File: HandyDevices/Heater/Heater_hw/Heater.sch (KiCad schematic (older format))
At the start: 41 parts

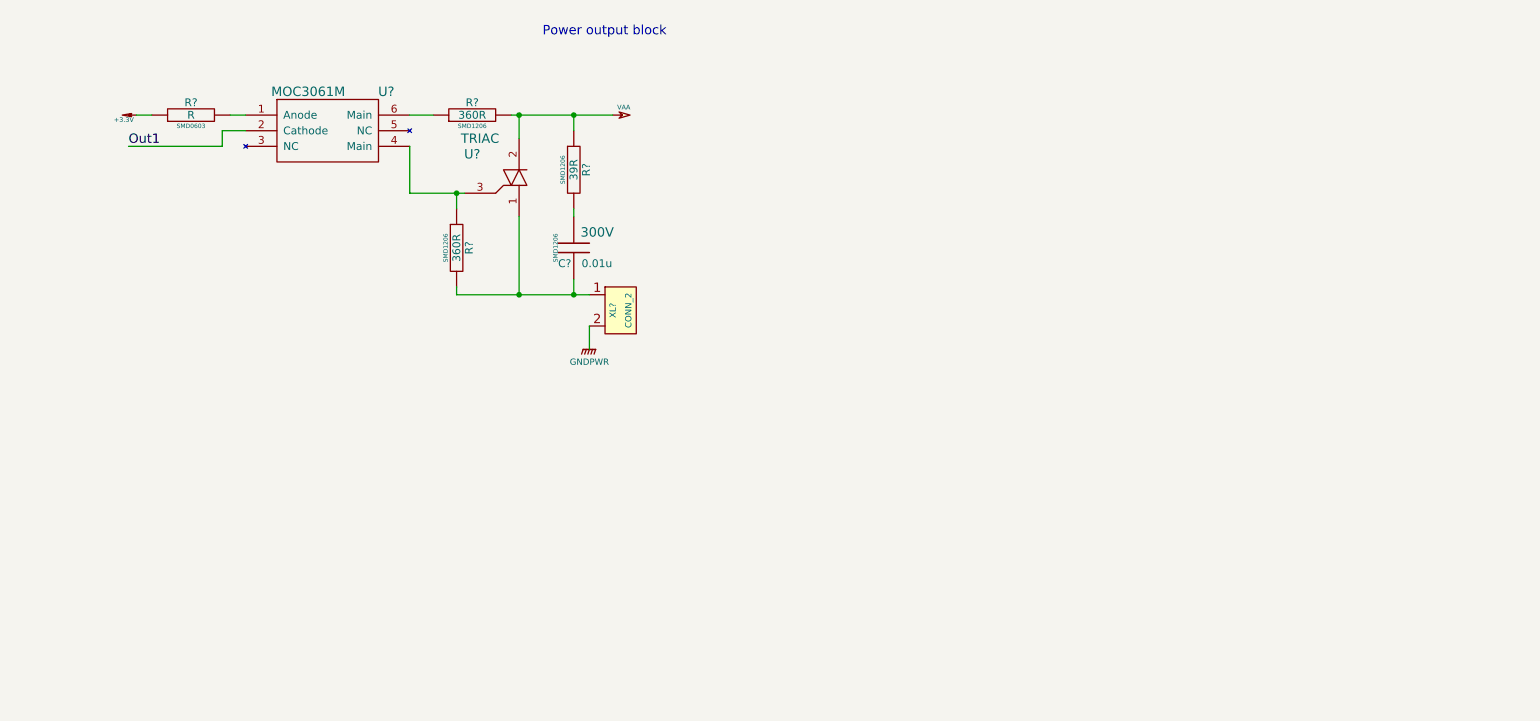
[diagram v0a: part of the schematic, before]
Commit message: 
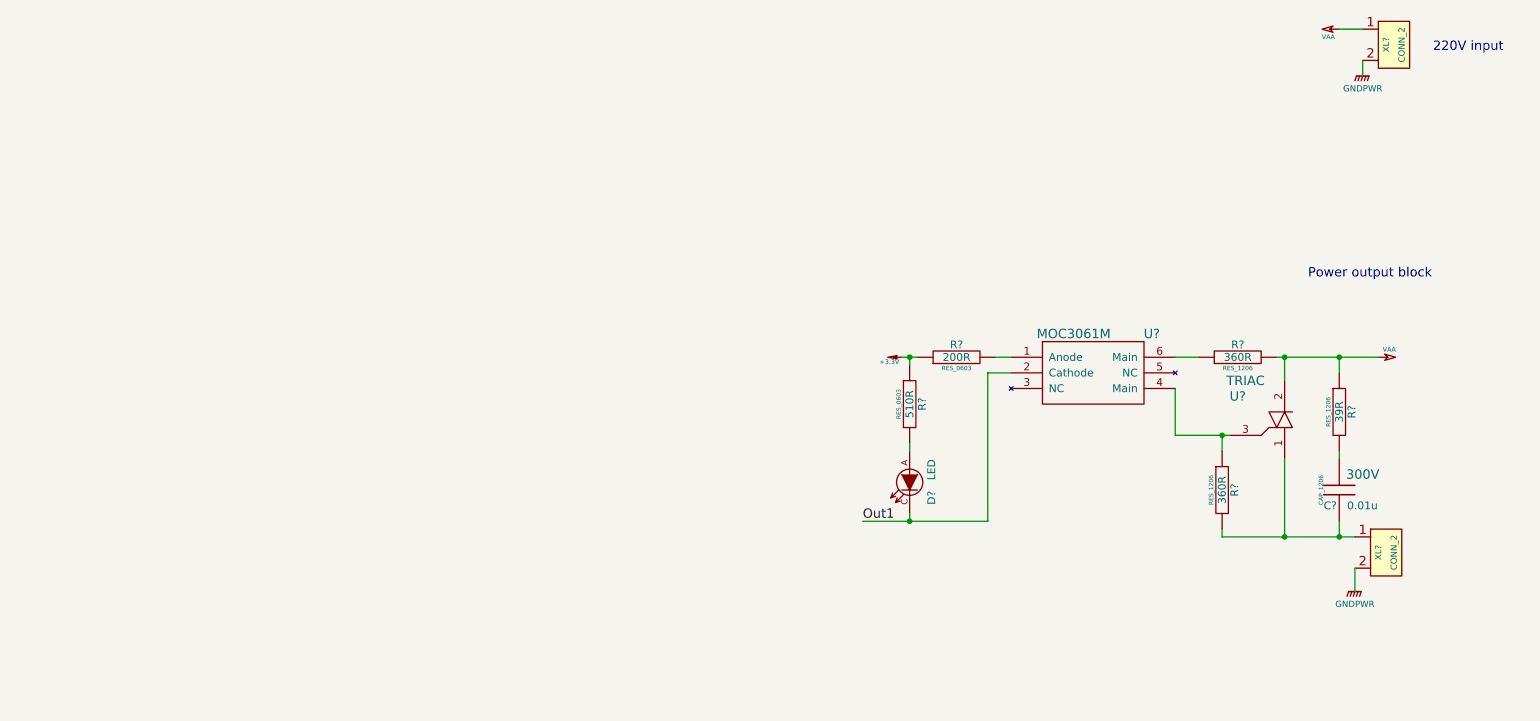
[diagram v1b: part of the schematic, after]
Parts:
- added D?: LED, symbol LED
- added R?: 510R, RES_0603, symbol R
- added XL?: CONN_2, symbol CONN_2
- C?: footprint SMD1206 -> CAP_1206
- R? (x3): footprint SMD1206 -> RES_1206
- R?: value R -> 200R; footprint SMD0603 -> RES_0603
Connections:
- net +3.3V: now also R?.1
- net GNDPWR: now also XL?.2 (PM)
- net Out1: now also D?.C
- net VAA: now also XL?.1 (P1)
- new net: D?.A, R?.2
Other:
- note added: "220V input"
- moved on the sheet: C?, R?, U?, XL?
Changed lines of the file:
@@
-EESchema Schematic File Version 2  date 09/07/2012 18:56:40
+EESchema Schematic File Version 2  date 10/07/2012 22:43:16
 LIBS:Connectors_kl
 LIBS:modules
@@
 LIBS:SmartCard_kl
 LIBS:Interface_kl
+LIBS:Heater-cache
 EELAYER 25  0
 EELAYER END
@@
 Sheet 1 1
 Title ""
-Date "9 jul 2012"
+Date "10 jul 2012"
 Rev ""
 Comp ""
@@
 Comment4 ""
 $EndDescr
-Wire Wire Line
-	13800 1750 13650 1750
-Wire Wire Line
-	13650 1750 13650 1850
-Wire Wire Line
-	13650 1850 13050 1850
-Wire Wire Line
-	13100 1650 13200 1650
-Wire Wire Line
-	14850 1650 15000 1650
-Wire Wire Line
-	15550 1650 15550 1800
-Wire Wire Line
-	15150 2150 15150 2250
-Connection ~ 15900 2800
-Wire Wire Line
-	15900 2800 15900 2700
-Wire Wire Line
-	16000 3000 16000 3150
+$Comp
+L R R?
+U 1 1 4FFBD56F
+P 18050 3500
+F 0 "R?" V 18130 3500 50  0000 C CNN
+F 1 "510R" V 18050 3500 50  0000 C CNN
+F 2 "RES_0603" V 17980 3500 28  0000 C CNN
+	1    18050 3500
+	1    0    0    -1
+$EndComp
+Wire Wire Line
+	18550 4250 18550 3300
+Wire Wire Line
+	17750 4250 18550 4250
+Wire Wire Line
+	18050 3750 18050 3800
+Wire Wire Line
+	20950 1300 20950 1400
+Wire Wire Line
+	18550 3300 18700 3300
+Wire Wire Line
+	18000 3200 18100 3200
+Wire Wire Line
+	19750 3200 19900 3200
+Wire Wire Line
+	20450 3200 20450 3350
+Wire Wire Line
+	20050 3700 20050 3800
+Connection ~ 20800 4350
+Wire Wire Line
+	20800 4350 20800 4250
+Wire Wire Line
+	20900 4550 20900 4700
 Wire Wire Line
 	7250 8400 7400 8400
@@
 	7400 8500 7250 8500
 Wire Wire Line
-	15900 2250 15900 2300
-Wire Wire Line
-	15900 1650 15900 1750
-Connection ~ 15900 1650
-Wire Wire Line
-	15150 2750 15150 2800
-Wire Wire Line
-	15150 2800 16000 2800
-Wire Wire Line
-	15550 2300 15550 2800
-Connection ~ 15550 2800
-Wire Wire Line
-	15500 1650 16150 1650
-Connection ~ 15550 1650
-Wire Wire Line
-	14850 1850 14850 2150
-Wire Wire Line
-	14850 2150 15200 2150
-Connection ~ 15150 2150
-Wire Wire Line
-	13700 1650 13800 1650
-Text Label 13050 1850 0    60   ~ 0
+	20800 3800 20800 3850
+Wire Wire Line
+	20800 3200 20800 3300
+Connection ~ 20800 3200
+Wire Wire Line
+	20050 4300 20050 4350
+Wire Wire Line
+	20050 4350 20900 4350
+Wire Wire Line
+	20450 3850 20450 4350
+Connection ~ 20450 4350
+Wire Wire Line
+	20400 3200 21050 3200
+Connection ~ 20450 3200
+Wire Wire Line
+	19750 3400 19750 3700
+Wire Wire Line
+	19750 3700 20100 3700
+Connection ~ 20050 3700
+Wire Wire Line
+	18600 3200 18700 3200
+Wire Wire Line
+	20800 1100 20950 1100
+Wire Wire Line
+	18050 3250 18050 3200
+Connection ~ 18050 3200
+Wire Wire Line
+	18050 4200 18050 4250
+Connection ~ 18050 4250
+$Comp
+L LED D?
+U 1 1 4FFBD513
+P 18050 4000
+F 0 "D?" H 18150 4140 50  0000 C CNN
+F 1 "LED" H 17970 4140 50  0000 C CNN
+	1    18050 4000
+	0    1    1    0
+$EndComp
+Text Notes 21400 1250 0    60   ~ 0
+220V input
+$Comp
+L VAA #PWR?
+U 1 1 4FFBCE99
+P 20800 1100
+F 0 "#PWR?" H 20800 1160 30  0001 C CNN
+F 1 "VAA" H 20870 1150 30  0000 C CNN
+	1    20800 1100
+	-1   0    0    1
+$EndComp
+$Comp
+L GNDPWR #PWR?
+U 1 1 4FFBCE91
+P 20950 1400
+F 0 "#PWR?" H 20950 1450 40  0001 C CNN
+F 1 "GNDPWR" H 20950 1320 40  0000 C CNN
+	1    20950 1400
+	1    0    0    -1
+$EndComp
+$Comp
+L CONN_2 XL?
+U 1 1 4FFBCE82
+P 21150 1200
+F 0 "XL?" V 21100 1200 40  0000 C CNN
+F 1 "CONN_2" V 21200 1200 40  0000 C CNN
+	1    21150 1200
+	1    0    0    -1
+$EndComp
+Text Label 17750 4250 0    60   ~ 0
 Out1
 $Comp
 L +3.3V #PWR?
 U 1 1 4FFAF0C3
-P 13100 1650
-F 0 "#PWR?" H 13100 1610 30  0001 C CNN
-F 1 "+3.3V" H 13180 1680 30  0000 C CNN
-	1    13100 1650
+P 18000 3200
+F 0 "#PWR?" H 18000 3160 30  0001 C CNN
+F 1 "+3.3V" H 18080 3230 30  0000 C CNN
+	1    18000 3200
 	-1   0    0    1
 $EndComp
@@
 L R R?
 U 1 1 4FFAF0B4
-P 13450 1650
-F 0 "R?" V 13530 1650 50  0000 C CNN
-F 1 "R" V 13450 1650 50  0000 C CNN
-F 2 "SMD0603" V 13380 1650 28  0000 C CNN
-	1    13450 1650
+P 18350 3200
+F 0 "R?" V 18430 3200 50  0000 C CNN
+F 1 "200R" V 18350 3200 50  0000 C CNN
+F 2 "RES_0603" V 18280 3200 28  0000 C CNN
+	1    18350 3200
 	0    -1   -1   0
 $EndComp
@@
 L OPTOCOUPLER_TR U?
 U 1 1 4FFAEFE1
-P 14300 1750
-F 0 "U?" H 14700 2000 60  0000 C CNN
-F 1 "MOC3061M" H 14200 2000 60  0000 C CNN
-	1    14300 1750
+P 19200 3300
+F 0 "U?" H 19600 3550 60  0000 C CNN
+F 1 "MOC3061M" H 19100 3550 60  0000 C CNN
+	1    19200 3300
 	1    0    0    -1
 $EndComp
@@
 L R R?
 U 1 1 4FFAEEDF
-P 15250 1650
-F 0 "R?" V 15330 1650 50  0000 C CNN
-F 1 "360R" V 15250 1650 50  0000 C CNN
-F 2 "SMD1206" V 15180 1650 28  0000 C CNN
-	1    15250 1650
+P 20150 3200
+F 0 "R?" V 20230 3200 50  0000 C CNN
+F 1 "360R" V 20150 3200 50  0000 C CNN
+F 2 "RES_1206" V 20080 3200 28  0000 C CNN
+	1    20150 3200
 	0    -1   -1   0
 $EndComp
@@
 L R R?
 U 1 1 4FFAEEA4
-P 15150 2500
-F 0 "R?" V 15230 2500 50  0000 C CNN
-F 1 "360R" V 15150 2500 50  0000 C CNN
-F 2 "SMD1206" V 15080 2500 28  0000 C CNN
-	1    15150 2500
+P 20050 4050
+F 0 "R?" V 20130 4050 50  0000 C CNN
+F 1 "360R" V 20050 4050 50  0000 C CNN
+F 2 "RES_1206" V 19980 4050 28  0000 C CNN
+	1    20050 4050
 	1    0    0    -1
 $EndComp
@@
 L TRIAC U?
 U 1 1 4FFAEE7C
-P 15550 2050
-F 0 "U?" H 15250 2200 60  0000 C CNN
-F 1 "TRIAC" H 15300 2300 60  0000 C CNN
-	1    15550 2050
+P 20450 3600
+F 0 "U?" H 20150 3750 60  0000 C CNN
+F 1 "TRIAC" H 20200 3850 60  0000 C CNN
+	1    20450 3600
 	1    0    0    -1
 $EndComp
@@
 L VAA #PWR?
 U 1 1 4FFAEAC1
-P 16150 1650
-F 0 "#PWR?" H 16150 1710 30  0001 C CNN
-F 1 "VAA" H 16220 1700 30  0000 C CNN
-	1    16150 1650
+P 21050 3200
+F 0 "#PWR?" H 21050 3260 30  0001 C CNN
+F 1 "VAA" H 21120 3250 30  0000 C CNN
+	1    21050 3200
 	1    0    0    -1
 $EndComp
@@
 L C C?
 U 1 1 4FFAEAAE
-P 15900 2500
-F 0 "C?" H 15800 2400 50  0000 L CNN
-F 1 "0.01u" H 15950 2400 50  0000 L CNN
-F 2 "SMD1206" V 15800 2500 28  0000 C BNN
-F 4 "300V" H 16050 2600 60  0000 C CNN "Umax"
-	1    15900 2500
+P 20800 4050
+F 0 "C?" H 20700 3950 50  0000 L CNN
+F 1 "0.01u" H 20850 3950 50  0000 L CNN
+F 2 "CAP_1206" V 20700 4050 28  0000 C BNN
+F 4 "300V" H 20950 4150 60  0000 C CNN "Umax"
+	1    20800 4050
 	1    0    0    -1
 $EndComp
@@
 L R R?
 U 1 1 4FFAEAAA
-P 15900 2000
-F 0 "R?" V 15980 2000 50  0000 C CNN
-F 1 "39R" V 15900 2000 50  0000 C CNN
-F 2 "SMD1206" V 15830 2000 28  0000 C CNN
-	1    15900 2000
+P 20800 3550
+F 0 "R?" V 20880 3550 50  0000 C CNN
+F 1 "39R" V 20800 3550 50  0000 C CNN
+F 2 "RES_1206" V 20730 3550 28  0000 C CNN
+	1    20800 3550
 	1    0    0    -1
 $EndComp
@@
 L GNDPWR #PWR?
 U 1 1 4FFAE70D
-P 16000 3150
-F 0 "#PWR?" H 16000 3200 40  0001 C CNN
-F 1 "GNDPWR" H 16000 3070 40  0000 C CNN
-	1    16000 3150
+P 20900 4700
+F 0 "#PWR?" H 20900 4750 40  0001 C CNN
+F 1 "GNDPWR" H 20900 4620 40  0000 C CNN
+	1    20900 4700
 	1    0    0    -1
 $EndComp
@@
 L CONN_2 XL?
 U 1 1 4FFAE6F9
-P 16200 2900
-F 0 "XL?" V 16150 2900 40  0000 C CNN
-F 1 "CONN_2" V 16250 2900 40  0000 C CNN
-	1    16200 2900
+P 21100 4450
+F 0 "XL?" V 21050 4450 40  0000 C CNN
+F 1 "CONN_2" V 21150 4450 40  0000 C CNN
+	1    21100 4450
 	1    0    0    -1
 $EndComp
@@
 	1    0    0    -1
 $EndComp
-Text Notes 15700 1150 0    60   ~ 0
+Text Notes 20600 2700 0    60   ~ 0
 Power output block
 $Comp

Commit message: 
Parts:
- added Q?: NPN, symbol NPN
- added R?: R, RES_0603, symbol R
- added R?: 10k, RES_0603, symbol R
- added XL?: CONN_2, symbol CONN_2
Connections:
- net +3.3V: now also Q?.3 (C), R?.1
- net GND: now also XL?.2 (PM)
- new net: Q?.1 (B), R?.2
- new net: Q?.2 (E), R?.1
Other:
- note added: "10k => 0.25mA"

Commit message: 
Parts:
- removed C1, C18, C8, C9: 1u, symbol C
- removed C11, C15: 1000pF, symbol C
- removed C2, C3, C4, C5, C6: 0.1u, symbol C
- removed C20: 10u, symbol C
- removed D3: LED, symbol LED
- removed DA10, DA5, DA6, DA7, DA8, DA9: PESD1CAN, symbol PESD1CAN
- removed DD1: STM32F100XX-64, symbol STM32F100XX-64
- removed L1: 10uH, symbol L
- removed R10: 220k, symbol R
- removed R6: 100R, symbol R
- removed R9: 300k, symbol R
- added BZ?: BUZZER, symbol BUZZER
- added C? (x3): 0.01u, CAP_1206, symbol C
- added C? (x4): 1u, CAP_0603, symbol C
- added C? (x2): 1000pF, CAP_0603, symbol C
- added C?: 10u, CAP_0805, symbol C
- added C? (x5): 0.1u, CAP_0603, symbol C
- added D? (x3): LED, symbol LED
- added DA? (x4): TL431_SO8, symbol TL431_SO8
- added DD?: STM32F10X-48, symbol STM32F10X-48
- added DD?: M24C04, symbol EEPROM_I2C
- added Q? (x3): BC817, symbol NPN
- added R? (x3): 510R, RES_0603, symbol R
- added R? (x6): 200R, RES_1206, symbol R
- added R? (x3): 200k, RES_1206, symbol R
- added R? (x3): 39R, RES_1206, symbol R
- added R?: 200k, RES_0603, symbol R
- added R?: 120k, RES_0603, symbol R
- added R? (x3): 10k, RES_0603, symbol R
- added R? (x3): 1k, RES_0603, symbol R
- added R? (x2): 4k7, symbol R
- added SW? (x4): BUTTON, symbol BUTTON
- added U? (x3): MOC3061M, symbol OPTOCOUPLER_TR
- added U? (x3): TRIAC, symbol TRIAC
- added XL? (x2): CONN_1, symbol CONN_1
- added XL? (x6): CONN_2, symbol CONN_2
- added XL?: CON_NOKIA_LCD, symbol CON_NOKIA_LCD
- Q?: value NPN -> BC817
- R?: value 360R -> 200k
- R?: value 360R -> 200R
- R?: footprint RES_0603 -> RES_1206
- R?: value R -> 1k
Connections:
- net +3.3V: now also C?.1, C?.1, C?.1, C?.1, C?.1, C?.1, C?.1, C?.1, C?.1, DD?.1 (VBAT), DD?.24 (VDD1), DD?.36 (VDD2), DD?.48 (VDD3), DD?.8 (Vcc), DD?.9 (VDDA), Q?.3 (C), Q?.3 (C), Q?.3 (C), R?.1, R?.1, R?.1, R?.1, R?.1, R?.1, R?.1, R?.1, R?.1, R?.1, R?.1, R?.2, XL?.10 (VDDI), XL?.9 (VDD)
- net GND: now also BZ?.2, C?.2, C?.2, C?.2, C?.2, C?.2, C?.2, C?.2, C?.2, C?.2, C?.2, DD?.1 (A0), DD?.2 (A1), DD?.23 (VSS1), DD?.3 (A2), DD?.35 (VSS2), DD?.4 (GND), DD?.44 (BOOT0), DD?.47 (VSS3), DD?.7 (WP), DD?.8 (VSSA), R?.2, SW?.1, SW?.1, SW?.1, SW?.1, XL?.2 (PM), XL?.2 (PM), XL?.2 (PM), XL?.3 (GND), XL?.7 (LED-)
- net GNDPWR: now also XL?.2 (PM), XL?.2 (PM), XL?.2 (PM)
- net Out1: now also DD?.19 (PB1/T3C4/ADC1-9)
- net Out2: now also D?.C, DD?.20 (PB2/BOOT1), U?.2 (Cathode)
- net Out3: now also D?.C, DD?.39 (PB3/JTDO), U?.2 (Cathode)
- net Out4: now also D?.C, DD?.40 (PB4/JTRST), U?.2 (Cathode)
- net SWCLK: now also DD?.37 (SWCLK/JTCK/PA14)
- net SWDIO: now also DD?.34 (SWDIO/JTMS/PA13)
- net UART_RX: now also DD?.31 (T1C3/RX1/PA10)
- net UART_TX: now also DD?.30 (T1C2/TX1/PA9)
- net VAA: now also R?.1, R?.1, R?.1, R?.2, R?.2, R?.2, U?.2 (A1), U?.2 (A1), U?.2 (A1), XL?.1 (P1); no longer XL?.1 (P1)
- net at DA3.7 (Feedback): now also C?.2, R?.1, R?.2
- net Out1_220: now reaches C?.2, R?.2, U?.1 (A2), XL?.1 (P1)
- net Ut1: now reaches XL?.1 (P1)
- net Ut1: now also R?.2, DA?.2 (A), DA?.3 (A), DA?.6 (A), DA?.7 (A)
- net at Q?.1 (B), R?.2: now also DA?.1 (C)
- net at Q?.2 (E), R?.1: now also DA?.8 (Ref)
- net +12V: no longer names the net of DA3.8 (In)
- net +12V: now also C?.1, C?.1
- net PWR_ERROR: no longer names the net of DA3.5 (~Error)
- new net: D?.A, R?.2 (x3)
- new net: R?.2, U?.1 (Anode) (x3)
- new net: R?.1, U?.3 (G), U?.4 (Main) (x3)
- new net: R?.1, U?.6 (Main) (x3)
- new net: C?.1, R?.2 (x3)
- new net: C?.2, DD?.18 (PB0/T3C3/ADC1-8)
- new net: DA?.1 (C), Q?.1 (B), R?.2 (x3)
- new net: DA?.8 (Ref), Q?.2 (E), R?.1 (x3)
- new net Btn1: DD?.41 (PB5), SW?.2
- new net Btn2: DD?.45 (PB8/T4C3), SW?.2
- new net Btn3: DD?.46 (PB9/T4C4), SW?.2
- new net Btn4: DD?.27 (PB14/MISO2), SW?.2
- new net I2C_SCL: DD?.42 (PB6/SCL1/T4C1), DD?.6 (SCL), R?.2
- new net I2C_SDA: DD?.43 (PB7/SDA1/T4C2), DD?.5 (SDA), R?.1
- new net In220: XL?.1 (P1), XL?.1 (P1)
- new net LCD_BCKLT: DD?.26 (PB13/SCK2), XL?.6 (LED+)
- new net LCD_SCLK: DD?.25 (PB12/CK3), XL?.1 (CLK)
- new net LCD_SDA: DD?.21 (PB10/SCL2/TX3), XL?.2 (DATA)
- new net LCD_XCS: DD?.28 (PB15/MOSI2), XL?.4 (CS)
- new net LCD_XRES: DD?.22 (PB11/SDA2/RX3), XL?.5 (RST)
- new net Out2_220: C?.2, R?.2, U?.1 (A2), XL?.1 (P1)
- new net Out3_220: C?.2, R?.2, U?.1 (A2), XL?.1 (P1)
- new net Out4_220: C?.2, R?.2, U?.1 (A2), XL?.1 (P1)
- new net Ut2: DA?.2 (A), DA?.3 (A), DA?.6 (A), DA?.7 (A), R?.2, XL?.1 (P1)
- new net Ut3: DA?.2 (A), DA?.3 (A), DA?.6 (A), DA?.7 (A), R?.2, XL?.1 (P1)
- new net Ut4: DA?.2 (A), DA?.3 (A), DA?.6 (A), DA?.7 (A), R?.2, XL?.1 (P1)
- no-connect marks 5 -> 4
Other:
- note added: "3.3V power regulator"
- note added: "I2C Addr = 1010 00(A8)"
- note added: "LCD"
- note added: "Outer fuse"
- note added: "Temperature to Voltage"
- note added: "Thermoresistor"
- note removed: "3.0V power regulator"
- note removed: "ESD protection"
- moved on the sheet: C?, D?, Q?, R?, U?, XL?
